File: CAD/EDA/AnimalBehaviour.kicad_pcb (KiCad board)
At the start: 2 copper layers, 104 x 83 mm, 26 parts, among them J1 SSR_INPUT, J10 Cam, J11 Imaging, J12 Conn_01x02_Male, J13 StimIsoIN, J2 SSR OUT, J3 StimCurrentInject, J4 StimIsoIN, J5 ImagingTrig, J6 CAM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

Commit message: Need opensuse.
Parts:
- J10, J11: footprint BhallaLab:Connector_Mini-DIN_Female_6Pin_2rows -> MD_60SM:CUI_MD-60SM
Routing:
- net AGND: track 372.3 -> 339.4 mm
- net ImagingTrig: track 31.2 -> 16.5 mm
- net CamTTL: track 25.6 -> 15.6 mm

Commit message: Version 20190707.pre1
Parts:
- J10, J11: footprint MD_60SM:CUI_MD-60SM -> MD-60SM:CUI_MD-60SM
- J5: value ImagingTrig -> Imaging
- J7: footprint Connector_Audio:Jack_3.5mm_CUI_SJ-3523-SMT_Horizontal -> BhallaLab:Jack_3.5mm_CUI_SJ1-3533NG_Horizontal
- RV1: value 1 MegOhm -> R_POT_TRIM; footprint Potentiometer_THT:Potentiometer_Alps_RK09L_Single_Vertical -> Potentiometer_THT:Potentiometer_Bourns_3296Y_Vertical
- ShockPad1: footprint TerminalBlock:TerminalBlock_Altech_AK300-2_P5.00mm -> BhallaLab:CUI_TB001-500-02BE
- moved J3 46.5 mm to (211.0, 70.0)
- moved J4 45.5 mm to (216.5, 94.0)
- moved J13 30.1 mm to (218.0, 82.0)
- moved RV1 28.5 mm to (206.5, 110.5), turned to 270 degrees
- moved J7 26.5 mm to (193.5, 44.5), turned to 0 degrees
- moved J2 16.8 mm to (203.5, 66.5)
- moved J11 2.24 mm to (139.5, 50.0)
- moved J10 2.21 mm to (165.5, 50.5)
- moved ShockPad1 0.71 mm to (216.0, 105.5), turned to 270 degrees
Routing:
- net ShockRelayCh34: track 52.0 -> 124.3 mm
- net EncB: track 65.2 -> 136.1 mm
- net EncA: track 69.2 -> 138.5 mm
- net ShockRelayCh12: track 56.2 -> 120.0 mm
- net TONE+: track 69.3 -> 31.0 mm
- net ShockPWM: track 69.8 -> 31.9 mm
- net OUT+: track 40.7 -> 11.3 mm
- net OUT-: track 44.1 -> 17.3 mm
- net AGND: track 339.4 -> 313.1 mm
- net PAD-: track 96.2 -> 71.4 mm
- net ShockRead: track 65.0 -> 86.7 mm
- net EX_5V: track 55.8 -> 39.1 mm
- net ShockStimIsolator: track 56.2 -> 72.1 mm
- net ImagingTrig: track 16.5 -> 29.8 mm
- net Net-(R2-Pad1): track 15.2 -> 24.4 mm
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
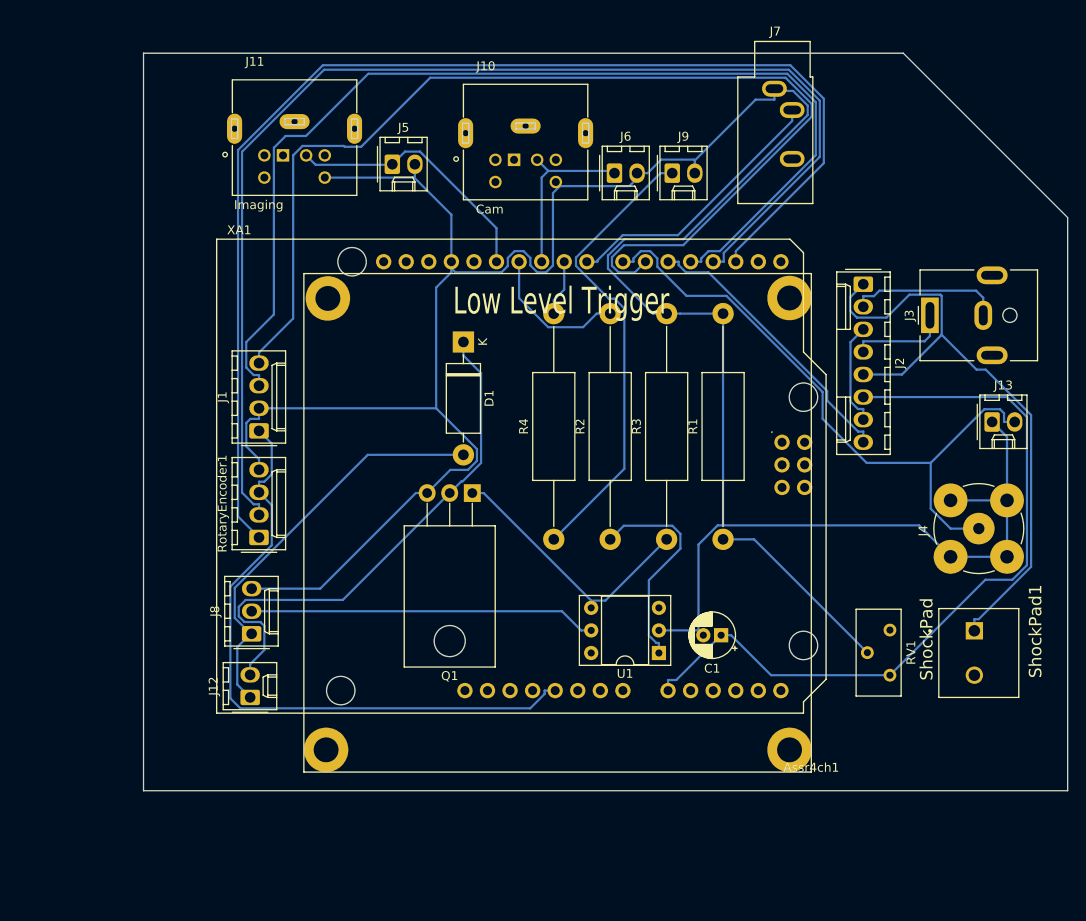
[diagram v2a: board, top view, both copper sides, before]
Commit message: rotated the pad and connector.
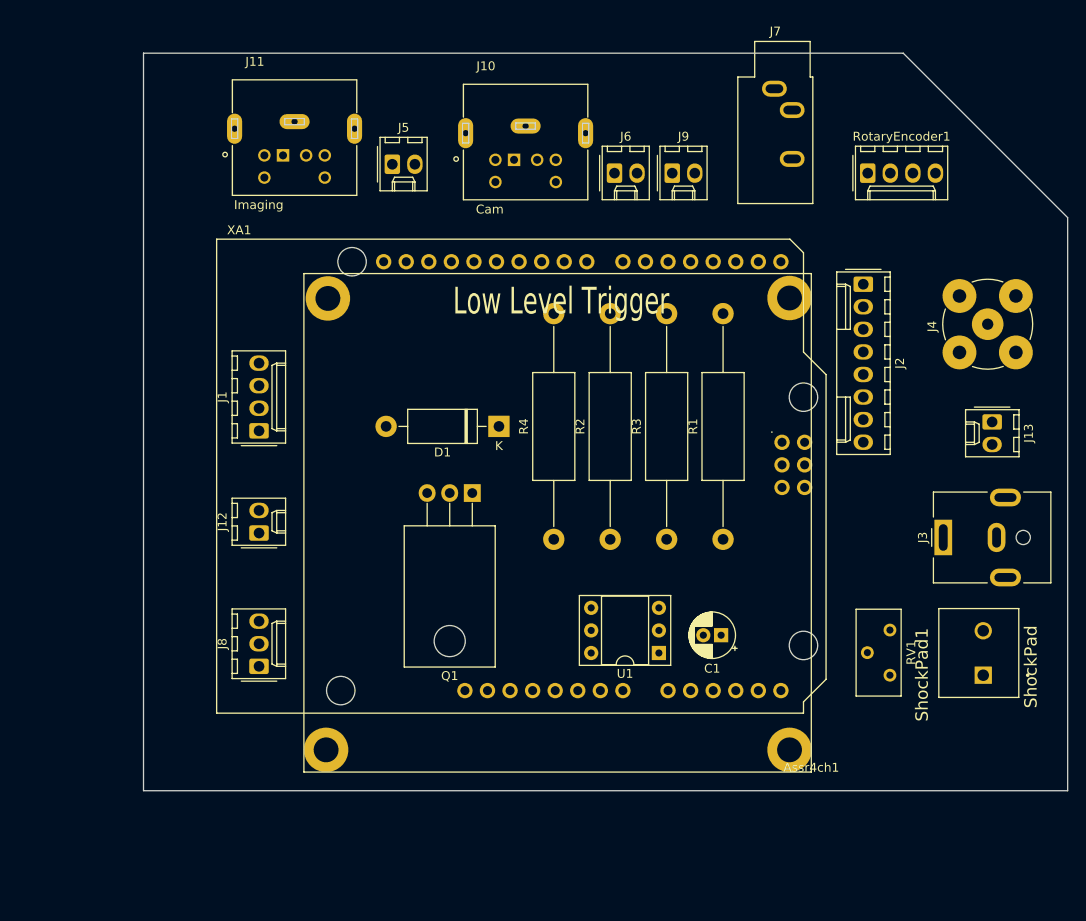
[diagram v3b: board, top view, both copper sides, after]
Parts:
- J12: value Conn_01x02_Male -> JSolenoid
- J8: value Conn_01x03_Male -> Ext Supp
- moved RotaryEncoder1 79.8 mm to (204.0, 54.0), turned to 0 degrees
- moved J3 25.0 mm to (212.5, 95.0)
- moved J4 23.0 mm to (217.5, 71.0)
- moved J12 18.5 mm to (135.5, 94.5)
- moved D1 10.3 mm to (162.5, 82.5), turned to 180 degrees
- moved ShockPad1 5.10 mm to (217.0, 110.5), turned to 90 degrees
- moved J8 3.75 mm to (135.5, 109.5)
- turned J13 to 270 degrees
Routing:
- net AGND: track 313.1 -> 0.00 mm
- net EncA: track 138.5 -> 0.00 mm
- net EncB: track 136.1 -> 0.00 mm
- net ShockRelayCh34: track 124.3 -> 0.00 mm
- net ShockRelayCh12: track 120.0 -> 0.00 mm
- net ShockRead: track 86.7 -> 0.00 mm
- net 5V: track 72.2 -> 0.00 mm
- net ShockStimIsolator: track 72.1 -> 0.00 mm
- net PAD-: track 71.4 -> 0.00 mm
- net Net-(D1-Pad1): track 59.0 -> 0.00 mm
- net Net-(J9-Pad1): track 52.4 -> 0.00 mm
- net EX_12V: track 46.3 -> 0.00 mm
- net EX_5V: track 39.1 -> 0.00 mm
- net ShockPWM: track 31.9 -> 0.00 mm
- net TONE+: track 31.0 -> 0.00 mm
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
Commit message: Aligned some components properly.
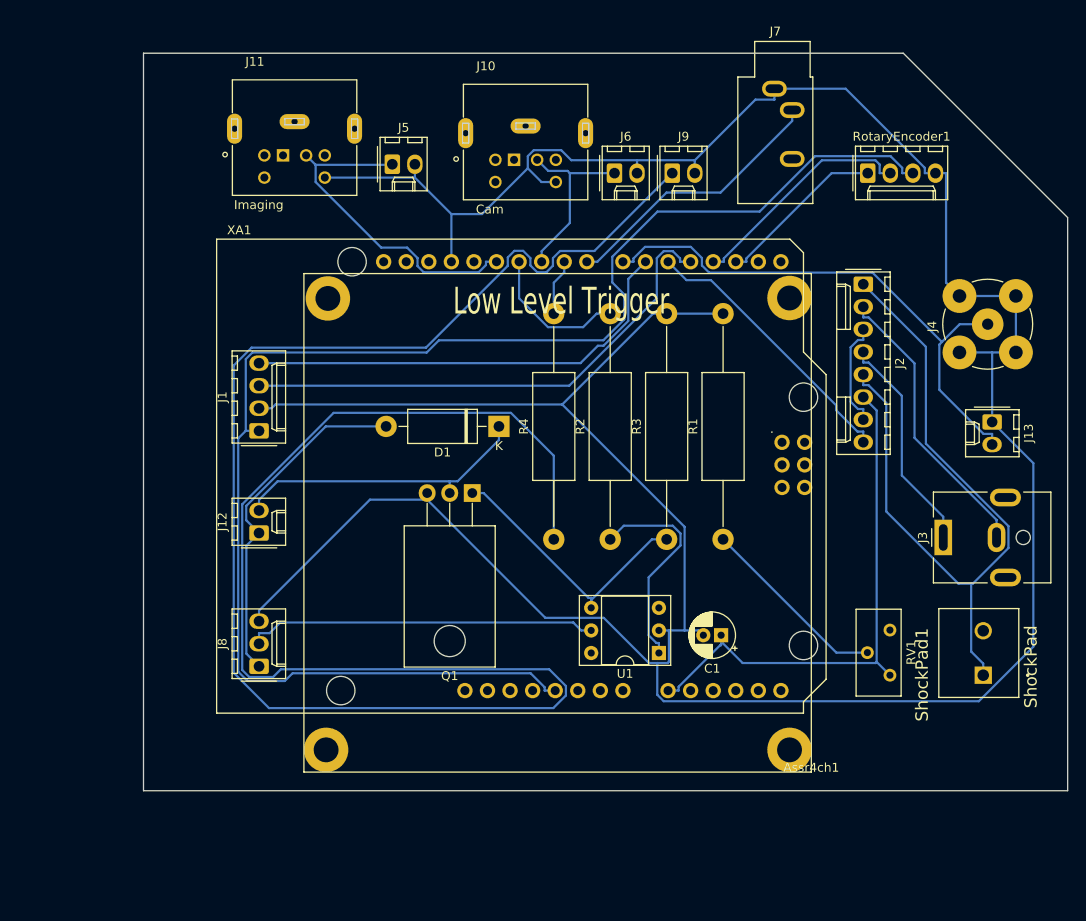
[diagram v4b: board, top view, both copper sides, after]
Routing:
- net AGND: track 0.00 -> 372.5 mm
- net Net-(J9-Pad1): track 0.00 -> 244.4 mm
- net 5V: track 0.00 -> 166.2 mm
- net PAD-: track 0.00 -> 82.9 mm
- net ShockStimIsolator: track 0.00 -> 62.4 mm
- net ShockRead: track 0.00 -> 60.6 mm
- net ShockRelayCh12: track 0.00 -> 58.2 mm
- net ShockRelayCh34: track 0.00 -> 51.0 mm
- net EX_5V: track 0.00 -> 39.4 mm
- net EX_12V: track 0.00 -> 39.3 mm
- net ImagingTrig: track 0.00 -> 37.9 mm
- net Net-(D1-Pad1): track 0.00 -> 33.8 mm
- net OUT-: track 0.00 -> 32.5 mm
- net ShockPWM: track 0.00 -> 31.4 mm
- net TONE+: track 0.00 -> 30.9 mm
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
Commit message: Fixed issues raised by @mrdorababu in #52.
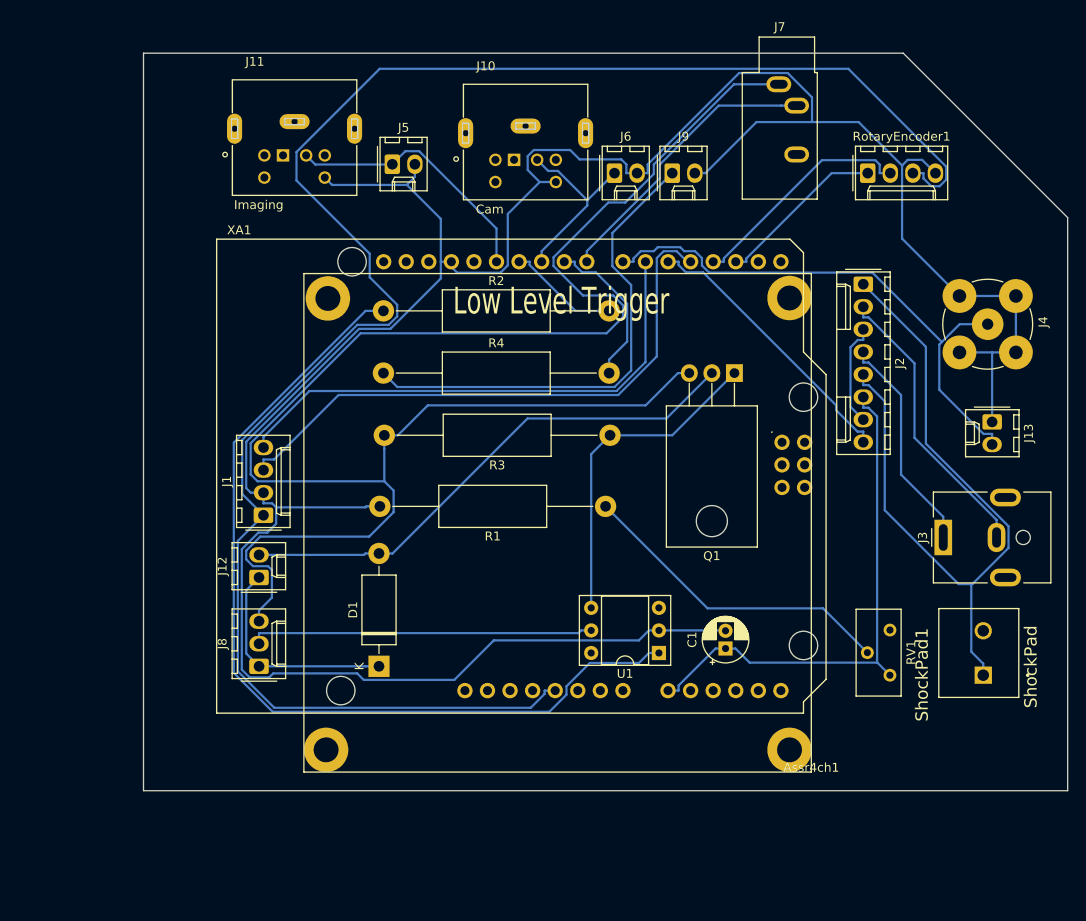
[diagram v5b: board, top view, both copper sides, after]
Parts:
- moved R2 36.2 mm to (149.5, 69.5), turned to 0 degrees
- moved Q1 32.4 mm to (189.0, 76.5)
- moved D1 30.2 mm to (149.0, 109.5), turned to 90 degrees
- moved R4 26.8 mm to (149.5, 76.5), turned to 0 degrees
- moved R1 13.7 mm to (174.5, 91.5), turned to 180 degrees
- moved R3 13.3 mm to (175.0, 83.5), turned to 180 degrees
- moved J1 9.51 mm to (136.0, 92.5)
- moved J12 5.00 mm to (135.5, 99.5)
- moved C1 1.58 mm to (188.0, 107.5), turned to 90 degrees
- moved J7 0.71 mm to (194.0, 44.0)
- turned J4 to 270 degrees
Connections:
- C1 pad 2: AGND -> DGND
- D1 pad 1: Net-(D1-Pad1) -> EX_12V
- D1 pad 2: EX_12V -> Net-(D1-Pad2)
- J1 pad 2: AGND -> DGND
- J10 pad 6: AGND -> DGND
- J11 pad 6: AGND -> DGND
- J12 pad 2: Net-(D1-Pad1) -> Net-(D1-Pad2)
- J13 pad 1: AGND -> DGND
- J4 pad 2: AGND -> DGND
- J5 pad 2: AGND -> DGND
- J6 pad 2: AGND -> DGND
- J9 pad 2: AGND -> DGND
- Q1 pad 2: Net-(D1-Pad1) -> Net-(D1-Pad2)
- R1 pad 2: AGND -> DGND
- RotaryEncoder1 pad 4: AGND -> DGND
- U1 pad 2: AGND -> DGND
- XA1 pad GND1: AGND -> DGND
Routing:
- net DGND: track 0.00 -> 298.7 mm
- net Net-(J9-Pad1): track 244.4 -> 55.2 mm
- net AGND: track 372.5 -> 188.1 mm
- net Net-(R2-Pad1): track 24.5 -> 101.8 mm
- net Net-(D1-Pad2): track 0.00 -> 59.4 mm
- net 5V: track 166.2 -> 201.1 mm
- net Net-(D1-Pad1): track 33.8 -> 0.00 mm
- net Net-(R1-Pad1): track 21.5 -> 36.3 mm
- net EX_12V: track 39.3 -> 24.7 mm
- net LED: track 6.33 -> 17.9 mm
- net ImagingTrig: track 37.9 -> 29.8 mm
- net ShockRelayCh34: track 51.0 -> 59.0 mm
- net ShockRelayCh12: track 58.2 -> 66.0 mm
- net Net-(Q1-Pad1): track 30.7 -> 37.2 mm
- net Puff: track 16.3 -> 12.6 mm
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
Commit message: Added ticket number and github issue. Added filled area so we don't remove too much Cu.
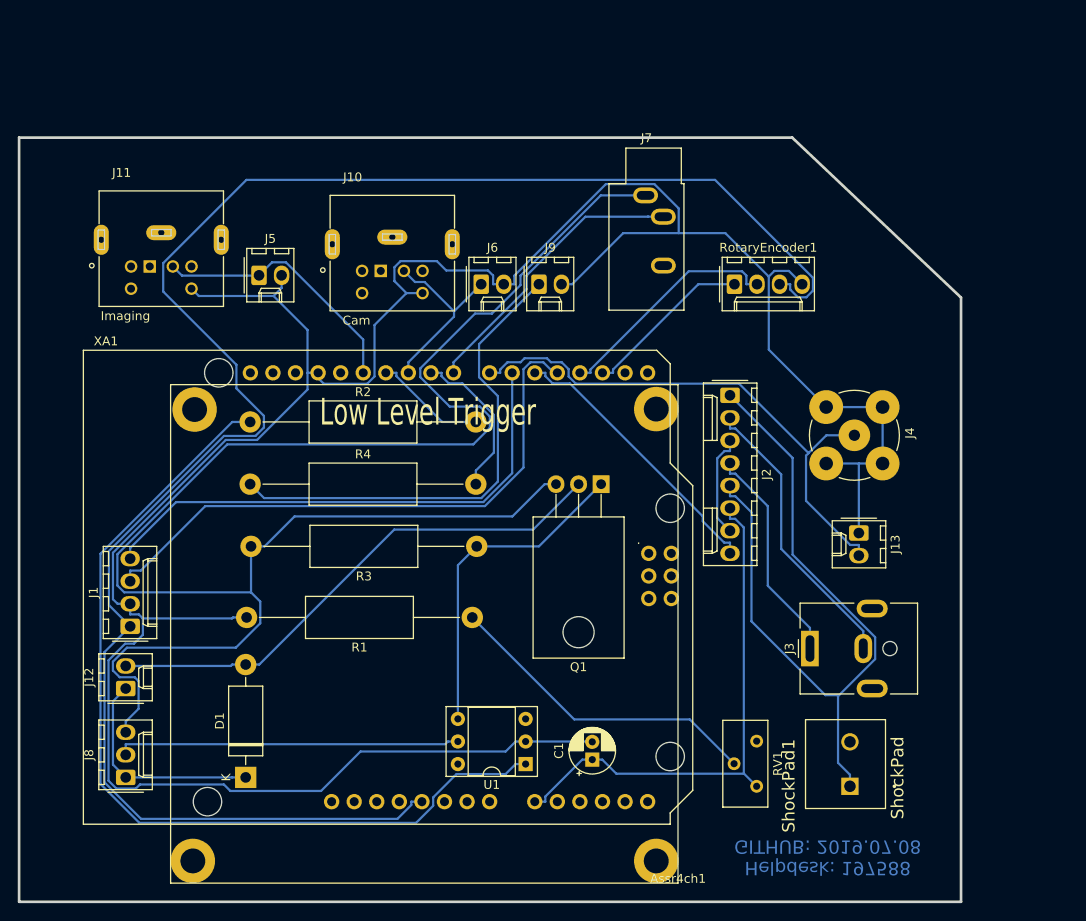
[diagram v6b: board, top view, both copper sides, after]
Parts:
- moved Assr4ch1 19.5 mm to (154.5, 107.5)
- moved C1 19.5 mm to (173.0, 120.0)
- moved D1 19.5 mm to (134.0, 122.0)
- moved J1 19.5 mm to (121.0, 105.0)
- moved J10 19.5 mm to (150.5, 63.0)
- moved J11 19.5 mm to (124.5, 62.5)
- moved J12 19.5 mm to (120.5, 112.0)
- moved J13 19.5 mm to (203.0, 94.5)
- moved J2 19.5 mm to (188.5, 79.0)
- moved J3 19.5 mm to (197.5, 107.5)
- moved J4 19.5 mm to (202.5, 83.5)
- moved J5 19.5 mm to (135.5, 65.5)
- moved J6 19.5 mm to (160.5, 66.5)
- moved J7 19.5 mm to (179.0, 56.5)
- moved J8 19.5 mm to (120.5, 122.0)
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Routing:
- added copper zone on B.Cu, net DGND
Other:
- board size 104 x 83 mm -> 106 x 86 mm
- board text added: "Helpdesk: 197588 GITHUB: 2019.07.08"

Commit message: replaced oval holes with circular holes.
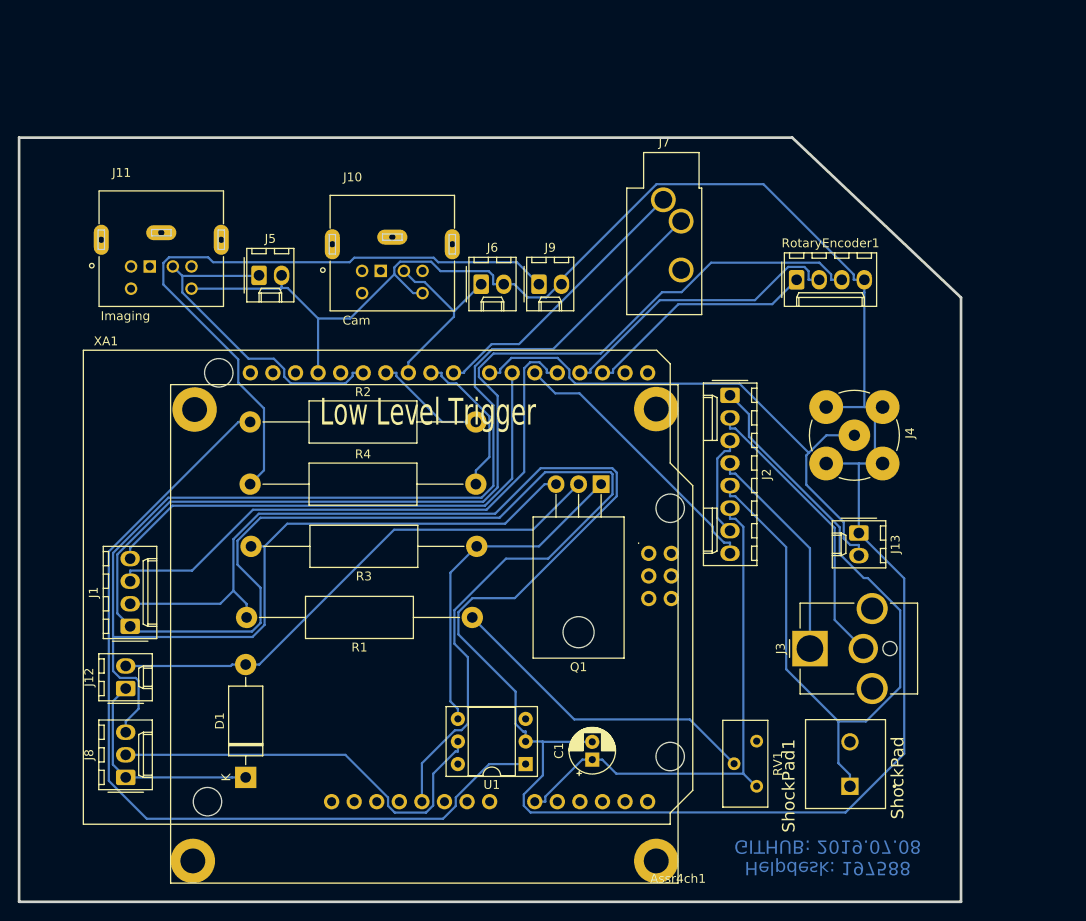
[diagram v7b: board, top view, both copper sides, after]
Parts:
- J3: footprint Connector_BarrelJack:BarrelJack_CUI_PJ-063AH_Horizontal -> Connector_BarrelJack:BarrelJack_CUI_PJ-063AH_Horizontal_CircularHoles
- J7: footprint BhallaLab:Jack_3.5mm_CUI_SJ1-3533NG_Horizontal -> Connector_Audio:Jack_3.5mm_CUI_SJ1-3533NG_Horizontal_CircularHoles
- moved RotaryEncoder1 7.02 mm to (196.0, 66.0)
- moved J7 2.06 mm to (181.0, 57.0)
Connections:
- J7 pad S: AGND -> TONE+
- J7 pad T: TONE+ -> AGND
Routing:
- net DGND: track 298.7 -> 346.3 mm
- net 5V: track 201.1 -> 237.2 mm
- net Net-(J9-Pad1): track 55.2 -> 74.4 mm
- net AGND: track 188.1 -> 176.9 mm
- net ImagingTrig: track 29.8 -> 37.8 mm
- net EX_5V: track 38.7 -> 46.7 mm
- net EncA: track 19.2 -> 26.4 mm
- net EncB: track 26.1 -> 33.3 mm
- net PAD-: track 82.9 -> 89.4 mm
- net Net-(R2-Pad1): track 101.8 -> 99.5 mm
- net LED: track 17.9 -> 17.1 mm
- net TONE+: track 32.5 -> 31.8 mm
- net Net-(Q1-Pad1): track 37.2 -> 37.9 mm
- net ShockRelayCh12: track 66.0 -> 66.5 mm

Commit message: temp commit. The layout is broken now.
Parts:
- moved J1 8.50 mm to (121.0, 96.5)
- moved J12 5.52 mm to (121.0, 106.5)
- moved J4 4.69 mm to (202.8, 78.8)
- moved J8 2.55 mm to (121.0, 119.5)
- moved D1 2.50 mm to (134.0, 119.5), turned to 0 degrees
- moved R4 2.46 mm to (133.5, 91.2)
- moved R3 2.24 mm to (159.0, 98.0)
- moved R2 1.41 mm to (133.5, 83.0)
- moved R1 0.56 mm to (159.0, 104.2)
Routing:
- net DGND: track 346.3 -> 0.00 mm
- net 5V: track 237.2 -> 0.00 mm
- net AGND: track 176.9 -> 0.00 mm
- net Net-(R2-Pad1): track 99.5 -> 0.00 mm
- net PAD-: track 89.4 -> 0.00 mm
- net Net-(J9-Pad1): track 74.4 -> 0.00 mm
- net ShockRelayCh12: track 66.5 -> 0.00 mm
- net ShockStimIsolator: track 62.4 -> 0.00 mm
- net Net-(D1-Pad2): track 59.4 -> 0.00 mm
- net ShockRead: track 59.4 -> 0.00 mm
- net ShockRelayCh34: track 59.3 -> 0.00 mm
- net EX_5V: track 46.7 -> 0.00 mm
- net Net-(Q1-Pad1): track 37.9 -> 0.00 mm
- net ImagingTrig: track 37.8 -> 0.00 mm
- net Net-(R1-Pad1): track 36.3 -> 0.00 mm
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- removed copper zone on B.Cu, net DGND
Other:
- net class Default: clearance 0.2 -> 0.4; trace_width 0.25 -> 0.4
- rule trace_clearance: 0.2 -> 0.4
